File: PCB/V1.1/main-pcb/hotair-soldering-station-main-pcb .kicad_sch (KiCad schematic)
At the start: 95 parts, among them J1 230VAC_IN, J10 SOLD_IRON (r.2,54), J11 LCD_CON2 (JST r.2.0), J12 LCD_CON1 (JST r.2.0), J13 ICP (goldpin r2,54), J2 FRONT_PANEL (IDC r. 2,54), J3 EARTH_GND, J4 24V_IN (NS-25 r2,54), J5 PSUPPLY (PWZ-02S r.3,96), J6 HOTAIR_FAN (JST r,2,54), J7 HOTAIR_MEAS (JST r.2,5), J8 HOTAIR_HEATER (PWZ-02S r.3,96), J9 SOLD_IRON (r.2,54), Q1 BC817, Q10 FP3055LP, Q11 BC817, Q2 BC807, Q3 BC817, Q4 Q_PMOS_GDS, Q5 BC817, Q6 BT139-600, Q7 BC817, Q8 FP3055LP, Q9 BC817, U1 MOC3041M, U2 MAX31855KASA, U3 MP1584-Step-Down, U4 AP1117-ADJ, U6 LM358, U7 MAX31855KASA, U8 STM32F103C6Tx

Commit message: PCB routing done
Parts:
- R14, R15: value 30k -> xx
- R4, R5: value 10k -> 100k
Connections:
- net +24V: now also Q4.3 (S); no longer Q4.2 (D)
- net FAN_SUPPLY: now also Q4.2 (D); no longer Q4.3 (S)
- net HOTAIR_UP_SW: now also U8.33 (PA12); no longer U8.28 (PB15)
- net MENU_DOWN_SW: now also U8.25 (PB12); no longer U8.33 (PA12)
- net MENU_OK_SW: now also U8.22 (PB11); no longer U8.32 (PA11)
- net SOLDER_DOWN_SW: now also U8.26 (PB13); no longer U8.25 (PB12)
- net SOLDER_ON_SW: now also U8.32 (PA11); no longer U8.21 (PB10)
- net SOLDER_SELECT_SW: now also U8.21 (PB10); no longer U8.26 (PB13)
- net SOLDER_UP_SW: now also U8.28 (PB15); no longer U8.22 (PB11)
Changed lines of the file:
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@@
     (stroke (width 0) (type default) (color 0 0 0 0))
   )
-  (wire (pts (xy 422.91 240.03) (xy 412.75 240.03))
+  (wire (pts (xy 422.91 240.03) (xy 412.115 240.03))
     (stroke (width 0) (type default) (color 0 0 0 0))
   )
@@
     )
   )
-  (global_label "SOLDER_UP_SW" (shape input) (at 412.75 234.95 180) (fields_autoplaced)
+  (global_label "SOLDER_UP_SW" (shape input) (at 412.75 245.11 180) (fields_autoplaced)
     (effects (font (size 1.27 1.27)) (justify right))
-    (property "Intersheet References" "${INTERSHEET_REFS}" (id 0) (at 0 0 0)
+    (property "Intersheet References" "${INTERSHEET_REFS}" (id 0) (at 0 10.16 0)
       (effects (font (size 1.27 1.27)) hide)
     )
@@
     )
   )
-  (global_label "HOTAIR_UP_SW" (shape input) (at 412.75 245.11 180) (fields_autoplaced)
-    (effects (font (size 1.27 1.27)) (justify right))
-    (property "Intersheet References" "${INTERSHEET_REFS}" (id 0) (at 0 0 0)
+  (global_label "HOTAIR_UP_SW" (shape input) (at 468.63 237.49 0) (fields_autoplaced)
+    (effects (font (size 1.27 1.27)) (justify left))
+    (property "Intersheet References" "${INTERSHEET_REFS}" (id 0) (at 881.38 482.6 0)
       (effects (font (size 1.27 1.27)) hide)
     )
@@
     )
   )
-  (global_label "SOLDER_DOWN_SW" (shape input) (at 412.75 237.49 180) (fields_autoplaced)
+  (global_label "SOLDER_DOWN_SW" (shape input) (at 412.115 240.03 180) (fields_autoplaced)
     (effects (font (size 1.27 1.27)) (justify right))
-    (property "Intersheet References" "${INTERSHEET_REFS}" (id 0) (at 0 0 0)
+    (property "Intersheet References" "${INTERSHEET_REFS}" (id 0) (at -0.635 2.54 0)
       (effects (font (size 1.27 1.27)) hide)
     )
@@
     )
   )
-  (global_label "SOLDER_SELECT_SW" (shape input) (at 412.75 240.03 180) (fields_autoplaced)
+  (global_label "SOLDER_SELECT_SW" (shape input) (at 412.75 232.41 180) (fields_autoplaced)
     (effects (font (size 1.27 1.27)) (justify right))
-    (property "Intersheet References" "${INTERSHEET_REFS}" (id 0) (at 0 0 0)
+    (property "Intersheet References" "${INTERSHEET_REFS}" (id 0) (at 0 -7.62 0)
       (effects (font (size 1.27 1.27)) hide)
     )
@@
     )
   )
-  (global_label "MENU_DOWN_SW" (shape input) (at 468.63 237.49 0) (fields_autoplaced)
-    (effects (font (size 1.27 1.27)) (justify left))
-    (property "Intersheet References" "${INTERSHEET_REFS}" (id 0) (at 0 0 0)
+  (global_label "MENU_DOWN_SW" (shape input) (at 412.75 237.49 180) (fields_autoplaced)
+    (effects (font (size 1.27 1.27)) (justify right))
+    (property "Intersheet References" "${INTERSHEET_REFS}" (id 0) (at 881.38 474.98 0)
       (effects (font (size 1.27 1.27)) hide)
     )
@@
     )
   )
-  (global_label "MENU_OK_SW" (shape input) (at 468.63 234.95 0) (fields_autoplaced)
-    (effects (font (size 1.27 1.27)) (justify left))
-    (property "Intersheet References" "${INTERSHEET_REFS}" (id 0) (at 0 0 0)
+  (global_label "MENU_OK_SW" (shape input) (at 412.75 234.95 180) (fields_autoplaced)
+    (effects (font (size 1.27 1.27)) (justify right))
+    (property "Intersheet References" "${INTERSHEET_REFS}" (id 0) (at 881.38 469.9 0)
       (effects (font (size 1.27 1.27)) hide)
     )
@@
     )
   )
-  (global_label "SOLDER_ON_SW" (shape input) (at 412.75 232.41 180) (fields_autoplaced)
-    (effects (font (size 1.27 1.27)) (justify right))
-    (property "Intersheet References" "${INTERSHEET_REFS}" (id 0) (at 0 0 0)
+  (global_label "SOLDER_ON_SW" (shape input) (at 468.63 234.95 0) (fields_autoplaced)
+    (effects (font (size 1.27 1.27)) (justify left))
+    (property "Intersheet References" "${INTERSHEET_REFS}" (id 0) (at 881.38 467.36 0)
       (effects (font (size 1.27 1.27)) hide)
     )
@@
       (effects (font (size 1.27 1.27)) (justify right))
     )
-    (property "Value" "10k" (id 1) (at 72.39 215.265 0)
+    (property "Value" "100k" (id 1) (at 73.66 215.9 0)
       (effects (font (size 1.27 1.27)) (justify right))
     )
@@
       (effects (font (size 1.27 1.27)) (justify right))
     )
-    (property "Value" "10k" (id 1) (at 85.725 214.63 0)
+    (property "Value" "100k" (id 1) (at 86.995 214.63 0)
       (effects (font (size 1.27 1.27)) (justify right))
     )
@@
       (effects (font (size 1.27 1.27)) (justify right))
     )
-    (property "Value" "30k" (id 1) (at 95.885 243.205 90)
+    (property "Value" "xx" (id 1) (at 95.885 243.205 90)
       (effects (font (size 1.27 1.27)) (justify right))
     )
@@
       (effects (font (size 1.27 1.27)) (justify right))
     )
-    (property "Value" "30k" (id 1) (at 95.885 253.365 90)
+    (property "Value" "xx" (id 1) (at 95.885 253.365 90)
       (effects (font (size 1.27 1.27)) (justify right))
     )
@@
     (pin "2")
   )
-  (symbol (lib_id "Device:Q_PMOS_GDS") (at 95.885 219.71 0) (unit 1)
+  (symbol (lib_id "Device:Q_PMOS_GDS") (at 95.885 219.71 0) (mirror x) (unit 1)
     (in_bom yes) (on_board yes)
-    (property "Reference" "Q4" (id 0) (at 101.092 218.5416 0)
+    (property "Reference" "Q4" (id 0) (at 101.092 220.8784 0)
       (effects (font (size 1.27 1.27)) (justify left))
     )
-    (property "Value" "Q_PMOS_GDS" (id 1) (at 101.092 220.853 0)
+    (property "Value" "Q_PMOS_GDS" (id 1) (at 101.092 218.567 0)
       (effects (font (size 1.27 1.27)) (justify left))
     )
-    (property "Footprint" "Power_Integrations:TO-220" (id 2) (at 100.965 217.17 0)
+    (property "Footprint" "Power_Integrations:TO-220" (id 2) (at 100.965 222.25 0)
       (effects (font (size 1.27 1.27)) hide)
     )
@@
     )
     (path "/00000000-0000-0000-0000-000060f777c2"
-      (reference "R4") (unit 1) (value "10k") (footprint "Capacitors:0805")
+      (reference "R4") (unit 1) (value "100k") (footprint "Capacitors:0805")
     )
     (path "/00000000-0000-0000-0000-000060fe3922"
-      (reference "R5") (unit 1) (value "10k") (footprint "Capacitors:0805")
+      (reference "R5") (unit 1) (value "100k") (footprint "Capacitors:0805")
     )
     (path "/00000000-0000-0000-0000-00005f7e13fc"
@@
     )
     (path "/00000000-0000-0000-0000-0000611770f2"
-      (reference "R14") (unit 1) (value "30k") (footprint "Capacitors:0805")
+      (reference "R14") (unit 1) (value "xx") (footprint "Capacitors:0805")
     )
     (path "/00000000-0000-0000-0000-00006117772e"
-      (reference "R15") (unit 1) (value "30k") (footprint "Capacitors:0805")
+      (reference "R15") (unit 1) (value "xx") (footprint "Capacitors:0805")
     )
     (path "/00000000-0000-0000-0000-000060dfb802"

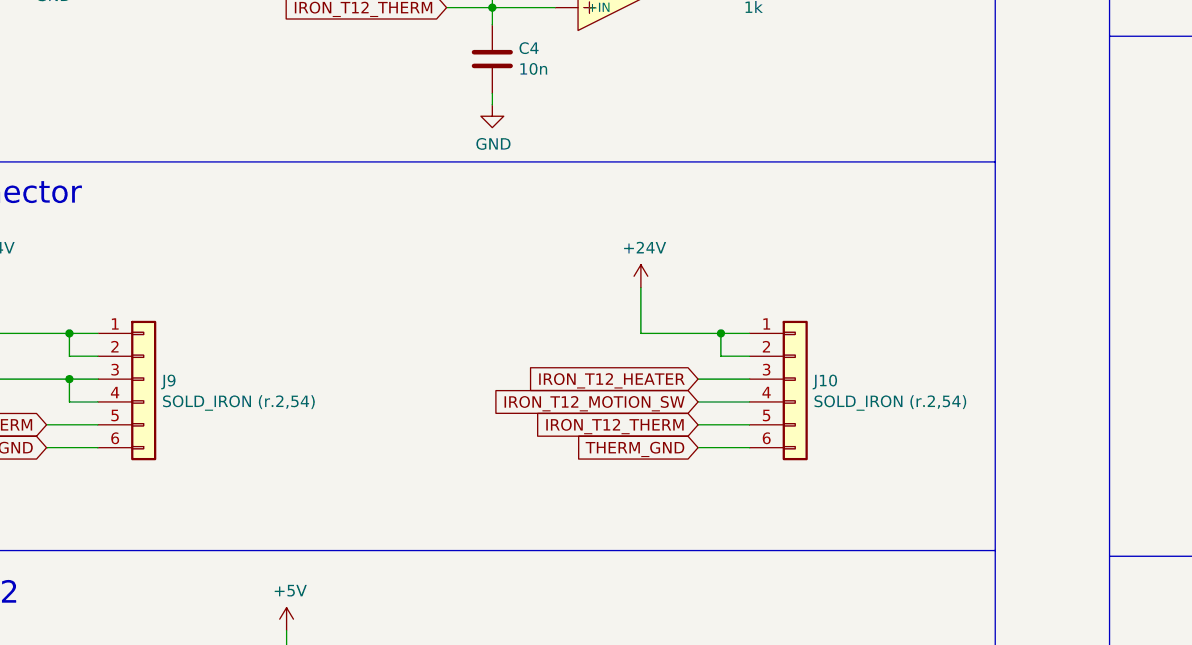
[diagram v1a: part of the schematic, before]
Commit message: Front panel V2, PCB text alignment, drill resize, T12 connector split
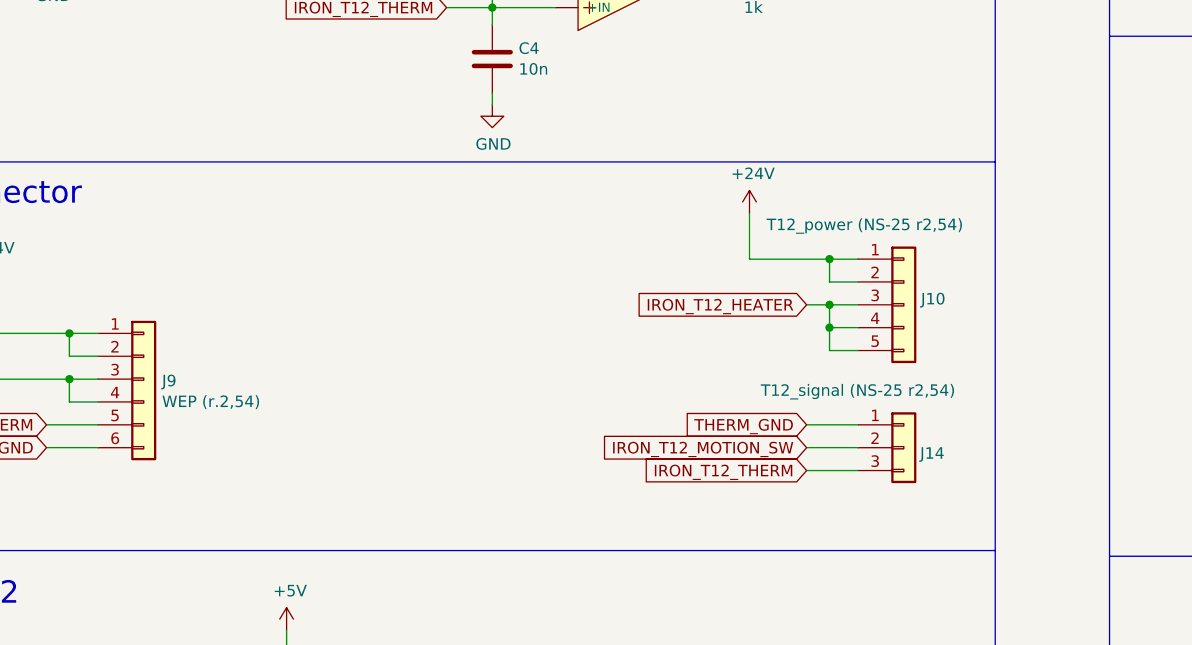
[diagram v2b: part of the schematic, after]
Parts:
- removed J10: SOLD_IRON (r.2,54), My-Footprints:Conn_1x06, symbol Connector_Generic:Conn_01x06
- added J10: T12_power (NS-25 r2,54), Connector:Conn-01x05-N25-W4P, symbol Connector_Generic:Conn_01x05
- added J14: T12_signal (NS-25 r2,54), Connector:Conn-01x03-N25-W4P, symbol Connector_Generic:Conn_01x03
- J4: footprint My-Footprints:Conn-01x04-N25-W4P -> My-Footprints:Conn-01x03-N25-W4P
- J9: value SOLD_IRON (r.2,54) -> WEP (r.2,54)
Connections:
- net +24V: now also J10.1 (Pin_1), J10.2 (Pin_2)
- net IRON_T12_HEATER: now also J10.3 (Pin_3), J10.4 (Pin_4), J10.5 (Pin_5)
- net IRON_T12_MOTION_SW: now also J14.2 (Pin_2)
- net IRON_T12_THERM: now also J14.3 (Pin_3)
- net THERM_GND: now also J14.1 (Pin_1)

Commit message: Fixing DRC violations
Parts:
- J4: footprint My-Footprints:Conn-01x03-N25-W4P -> My-Footprints:Conn-01x04-N25-W4P
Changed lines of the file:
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@@
     (property "Reference" "J4" (id 0) (at 38.1 90.17 0))
     (property "Value" "24V_IN (NS-25 r2,54)" (id 1) (at 33.02 106.045 0))
-    (property "Footprint" "My-Footprints:Conn-01x03-N25-W4P" (id 2) (at 38.735 100.33 0)
+    (property "Footprint" "My-Footprints:Conn-01x04-N25-W4P" (id 2) (at 38.735 100.33 0)
       (effects (font (size 1.27 1.27)) hide)
     )
@@
     )
     (path "/00000000-0000-0000-0000-00005f902970"
-      (reference "J4") (unit 1) (value "24V_IN (NS-25 r2,54)") (footprint "My-Footprints:Conn-01x03-N25-W4P")
+      (reference "J4") (unit 1) (value "24V_IN (NS-25 r2,54)") (footprint "My-Footprints:Conn-01x04-N25-W4P")
     )
     (path "/00000000-0000-0000-0000-00005fad2edb"

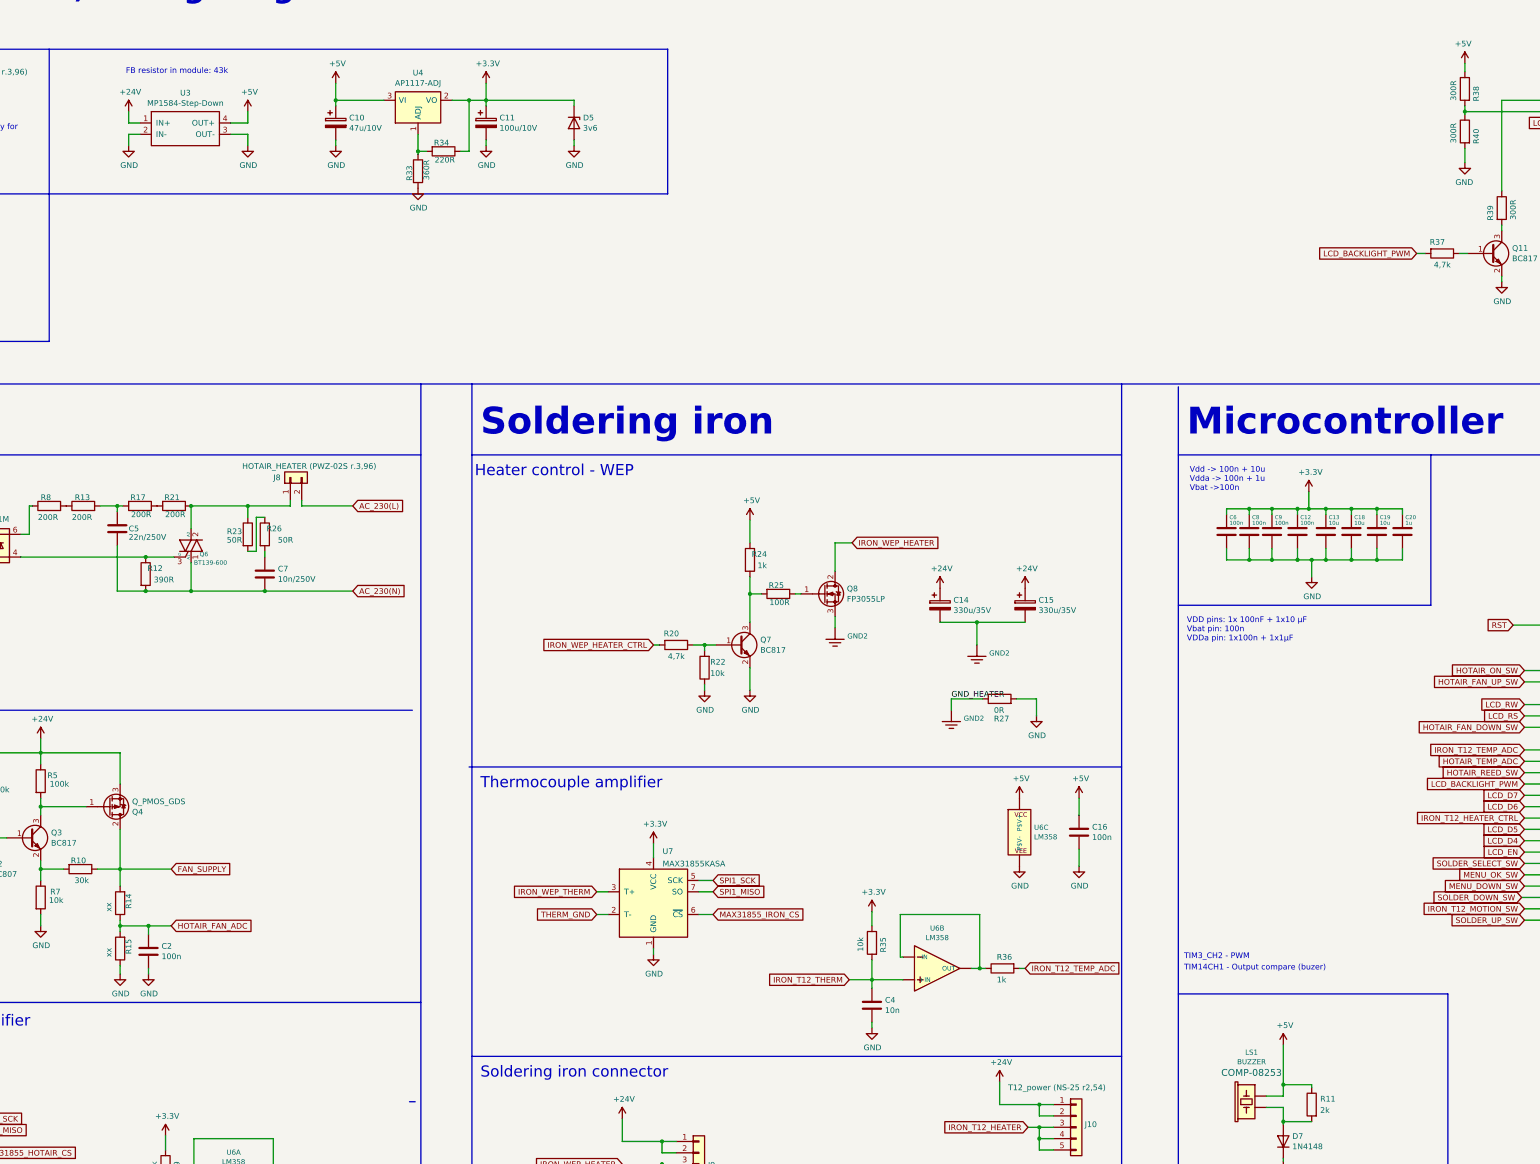
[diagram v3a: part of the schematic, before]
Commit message: Configure STM32F1 uC. Fix reset pin and UART problems.
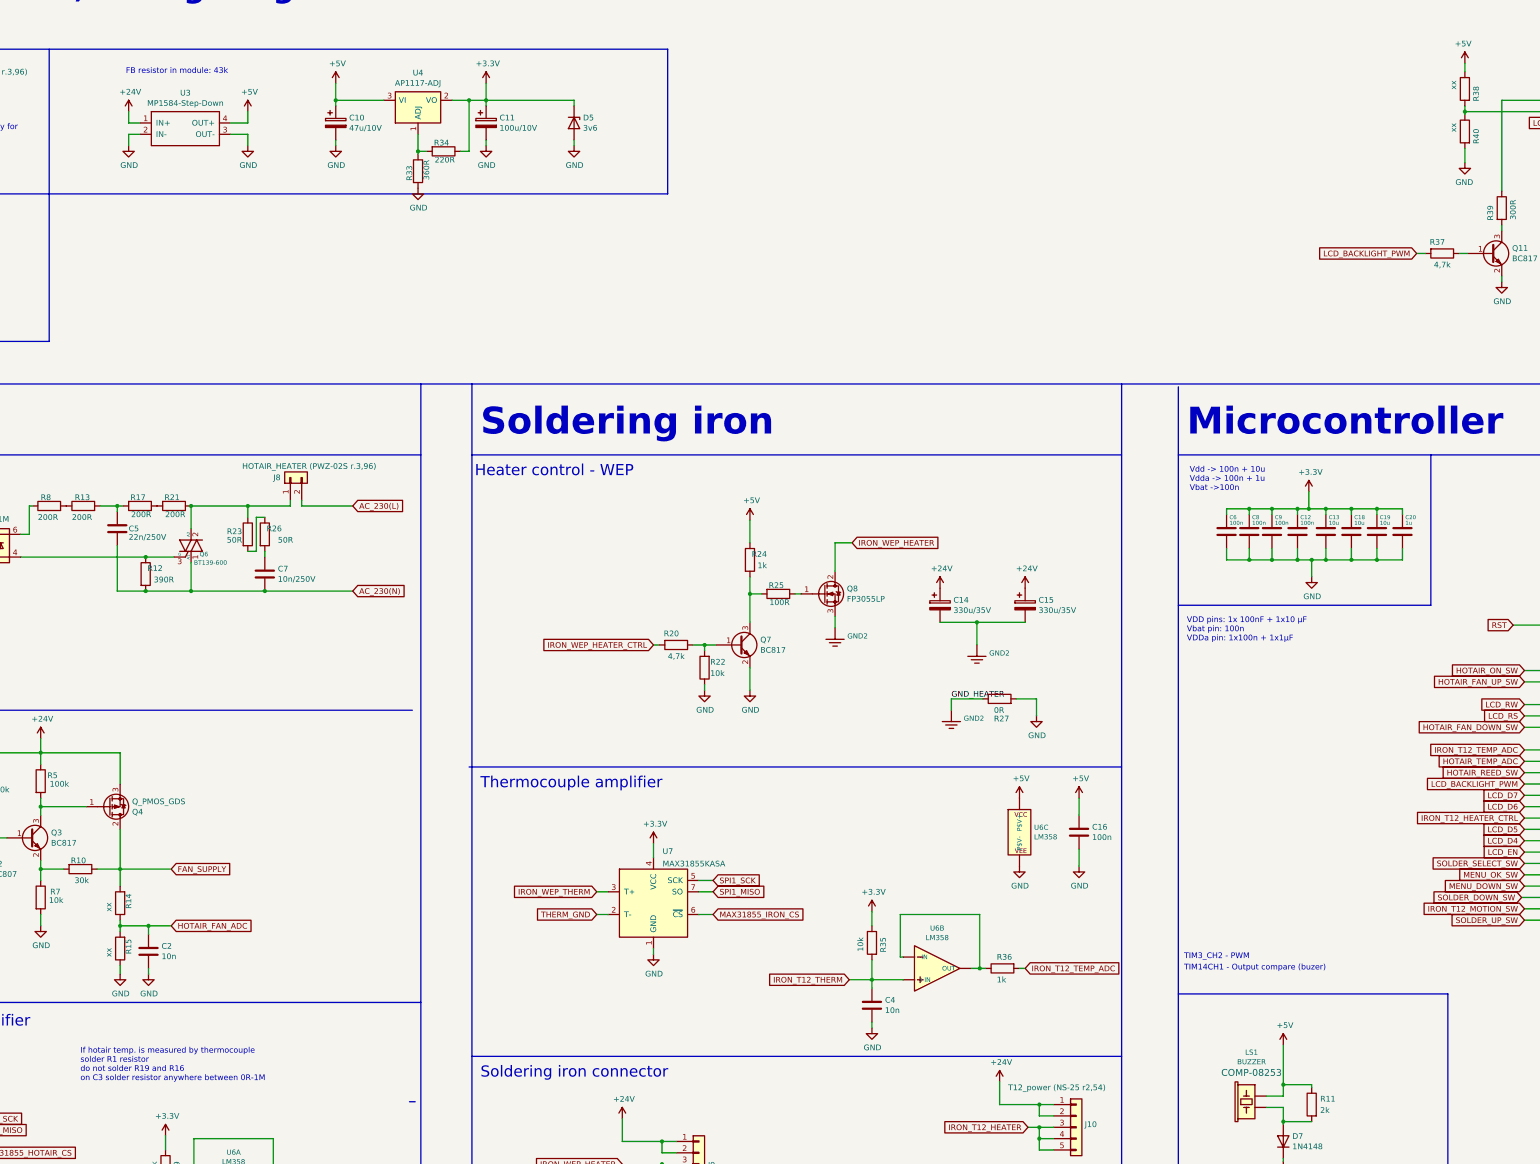
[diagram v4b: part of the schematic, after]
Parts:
- C2: value 100n -> 10n
- J2: footprint My-Footprints:Conn-01x14 -> My-Footprints:Conn-01x14-IDC
- R38, R40: value 300R -> xx
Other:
- note added: "If hotair temp. is measured by thermocouple solder R1 resistor do not solder R19 and R16 on C3 solder resistor anywhere between 0R-1M"
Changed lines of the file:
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@@
     (effects (font (size 5.9944 5.9944) (thickness 1.1989) bold) (justify left bottom))
   )
+  (text "If hotair temp. is measured by thermocouple\nsolder R1 resistor\ndo not solder R19 and R16\non C3 solder resistor anywhere between 0R-1M"
+    (at 89.535 281.305 0)
+    (effects (font (size 1.27 1.27)) (justify left bottom))
+  )
   (text "Thermocouple amplifier" (at 179.07 215.9 0)
     (effects (font (size 2.4892 2.4892)) (justify left bottom))
@@
     (property "Reference" "J2" (id 0) (at 523.875 65.6082 0))
     (property "Value" "FRONT_PANEL (IDC r. 2,54)" (id 1) (at 525.145 67.945 0))
-    (property "Footprint" "My-Footprints:Conn-01x14" (id 2) (at 522.605 78.74 0)
+    (property "Footprint" "My-Footprints:Conn-01x14-IDC" (id 2) (at 522.605 78.74 0)
       (effects (font (size 1.27 1.27)) hide)
     )
@@
       (effects (font (size 1.27 1.27)) (justify left))
     )
-    (property "Value" "100n" (id 1) (at 107.696 253.238 0)
+    (property "Value" "10n" (id 1) (at 107.696 253.238 0)
       (effects (font (size 1.27 1.27)) (justify left))
     )
@@
       (effects (font (size 1.27 1.27)) (justify right))
     )
-    (property "Value" "300R" (id 1) (at 396.875 57.15 90)
+    (property "Value" "xx" (id 1) (at 396.875 57.15 90)
       (effects (font (size 1.27 1.27)) (justify right))
     )
@@
       (effects (font (size 1.27 1.27)) (justify right))
     )
-    (property "Value" "300R" (id 1) (at 396.875 66.675 90)
+    (property "Value" "xx" (id 1) (at 396.875 66.675 90)
       (effects (font (size 1.27 1.27)) (justify right))
     )
@@
     )
     (path "/00000000-0000-0000-0000-000060e4b0d9"
-      (reference "C2") (unit 1) (value "100n") (footprint "Capacitors:0805")
+      (reference "C2") (unit 1) (value "10n") (footprint "Capacitors:0805")
     )
     (path "/00000000-0000-0000-0000-00006129441a"
@@
     )
     (path "/00000000-0000-0000-0000-00005f813d31"
-      (reference "J2") (unit 1) (value "FRONT_PANEL (IDC r. 2,54)") (footprint "My-Footprints:Conn-01x14")
+      (reference "J2") (unit 1) (value "FRONT_PANEL (IDC r. 2,54)") (footprint "My-Footprints:Conn-01x14-IDC")
     )
     (path "/00000000-0000-0000-0000-00005f97bd89"
@@
     )
     (path "/00000000-0000-0000-0000-000061c9824b"
-      (reference "R38") (unit 1) (value "300R") (footprint "Capacitors:0805")
+      (reference "R38") (unit 1) (value "xx") (footprint "Capacitors:0805")
     )
     (path "/00000000-0000-0000-0000-000061c4bdf0"
@@
     )
     (path "/4e1612ff-a765-47e6-b496-7d3286644f48"
-      (reference "R40") (unit 1) (value "300R") (footprint "Capacitors:0805")
+      (reference "R40") (unit 1) (value "xx") (footprint "Capacitors:0805")
     )
     (path "/00000000-0000-0000-0000-00005f7da3cf"
